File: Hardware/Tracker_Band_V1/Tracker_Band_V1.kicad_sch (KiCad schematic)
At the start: 30 parts, among them J1 USB_C_USB20, SW1 EVP-AVAA1A, SW2 EVP-AVAA1A, U1 ESP32-C3-MINI-1-N4, U2 BNO085, U3 RT8010, U4 MCP73832-2-AC, U5 LM66200, U6 IN-PI15TAT5R5G5B, X1 32.768kHz

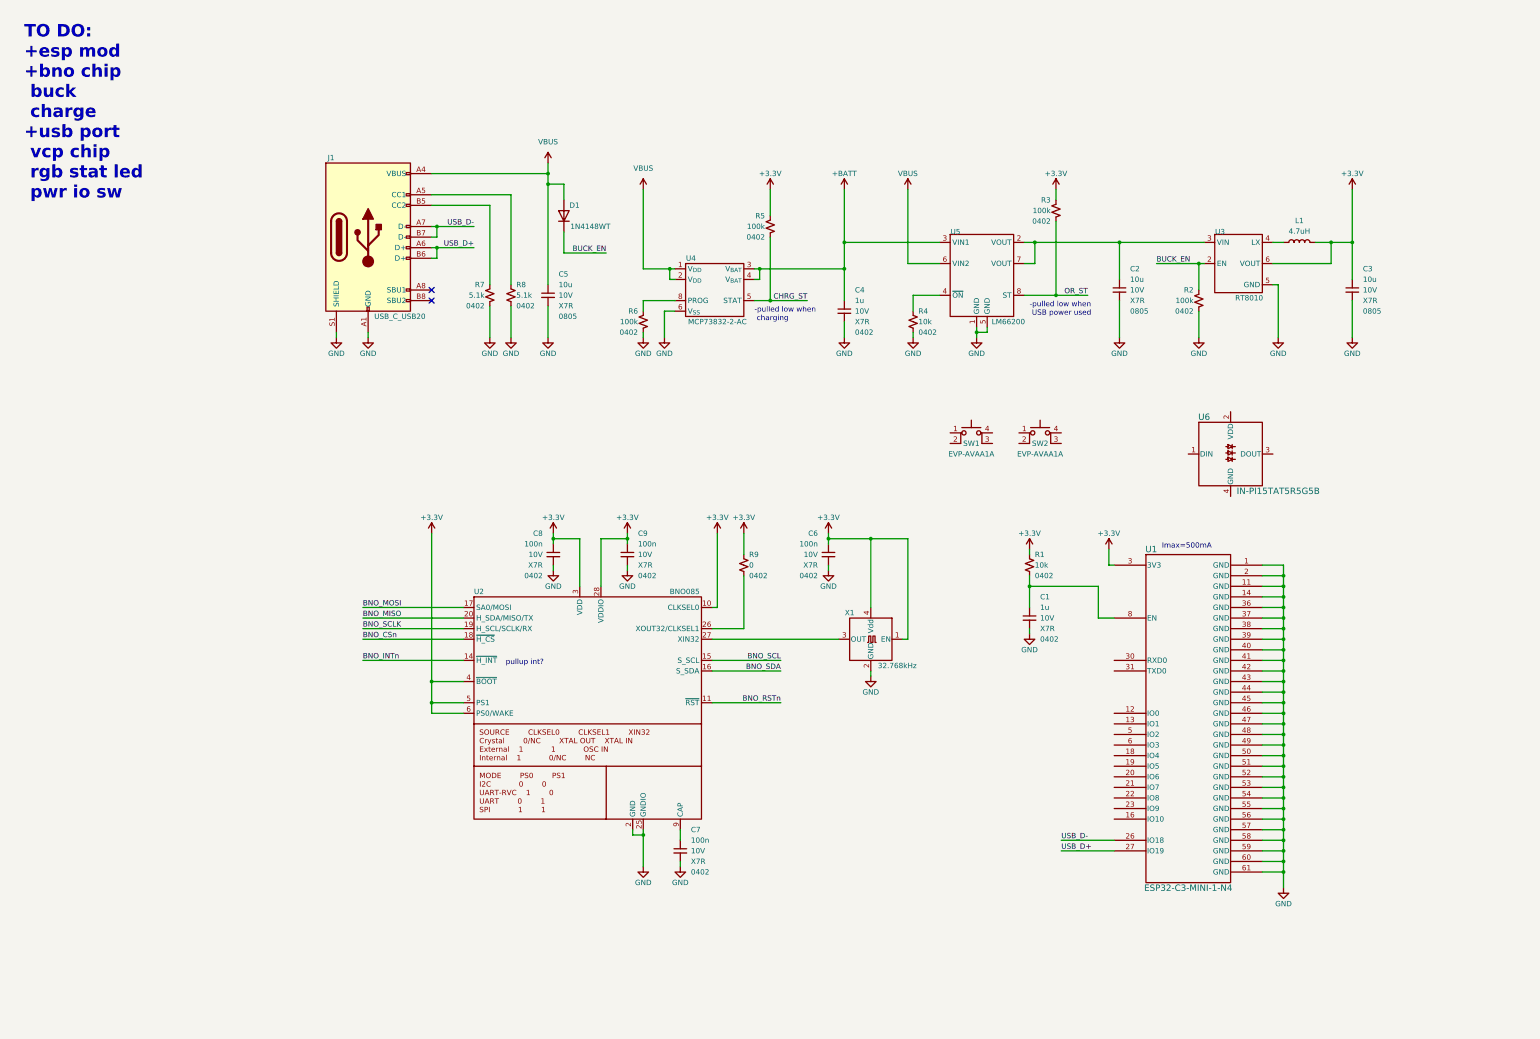
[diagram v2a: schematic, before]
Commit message: Schematic ready for layout
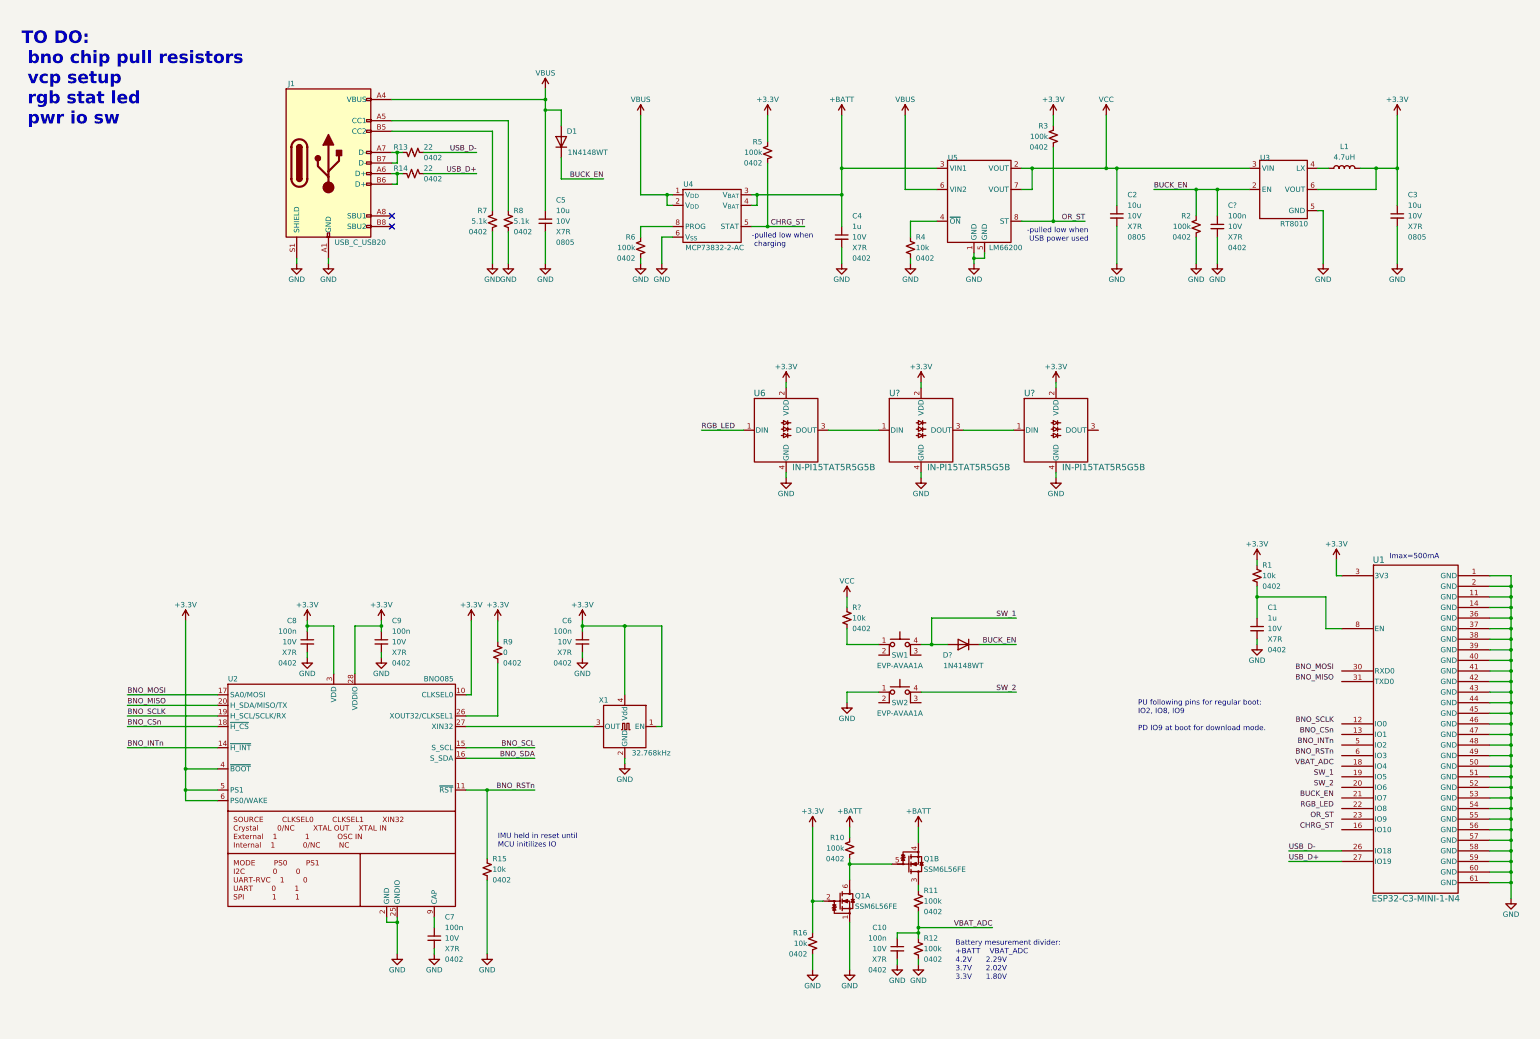
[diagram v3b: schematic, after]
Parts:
- added C10, C?: 100n, Capacitor_SMD:C_0402_1005Metric, symbol Device:C_Small
- added D?: 1N4148WT, Diode_SMD:D_SOD-523, symbol Diode:1N4148WT
- added Q1: SSM6L56FE, Package_TO_SOT_SMD:SOT-563, symbol 00_tracker_sym:SSM6L56FE
- added R10, R11, R12: 100k, Resistor_SMD:R_0402_1005Metric, symbol Device:R_Small_US
- added R13, R14: 22, Resistor_SMD:R_0402_1005Metric, symbol Device:R_Small_US
- added R15, R16, R?: 10k, Resistor_SMD:R_0402_1005Metric, symbol Device:R_Small_US
- added U? (x2): IN-PI15TAT5R5G5B, 00_tracker_fp:IN-PI15_INL, symbol 00_tracker_sym:IN-PI15TAT5R5G5B
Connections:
- net +3.3V: now also U6.2 (VDD), Q1.2 (G), R16.1, U?.2 (VDD), U?.2 (VDD)
- net +BATT: now also Q1.4 (1), R10.1
- net BNO_RSTn: now also R15.1
- net BUCK_EN: now also C?.1, D?.1 (K)
- net GND: now also SW2.1, U6.4 (GND), C10.2, C?.2, Q1.1 (S), R12.2, R15.2, R16.2, U?.4 (GND), U?.4 (GND)
- net USB_D+: now also R14.2; no longer J1.A6 (D+), J1.B6 (D+)
- net USB_D-: now also R13.2; no longer J1.A7 (D-), J1.B7 (D-)
- net SW_2: now reaches SW2.4 (A)
- net VCC: now reaches C2.1, U3.3 (VIN), U5.2 (VOUT), U5.7 (VOUT)
- net VCC: now also R?.1
- net at SW1.1: now also R?.2
- net SW_1: now reaches SW1.4 (A)
- net SW_1: now also D?.2 (A)
- net RGB_LED: now reaches U6.1 (DIN)
- net at U6.3 (DOUT): now also U?.1 (DIN)
- new net: Q1.3 (D), R11.1
- new net: Q1.5 (G), Q1.6 (D), R10.2
- new net: J1.A6 (D+), J1.B6 (D+), R14.1
- new net: J1.A7 (D-), J1.B7 (D-), R13.1
- new net: U?.1 (DIN), U?.3 (DOUT)
- new net VBAT_ADC: C10.1, R11.2, R12.1
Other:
- note added: "Battery mesurement divider: +BATT VBAT_ADC 4.2V 2.29V 3.7V 2.02V 3.3V 1.80V"
- note added: "IMU held in reset until MCU initilizes IO"
- note added: "PU following pins for regular boot: IO2, IO8, IO9 PD IO9 at boot for download mode."
- note added: "TO DO: bno chip pull resistors vcp setup rgb stat led pwr io sw"
- note removed: "TO DO: +esp mod +bno chip buck charge +usb port vcp chip rgb stat led pwr io sw"
- note removed: "pullup int?"
- moved on the sheet: C1, C2, C3, C4, C5, C6, C7, C8, C9, D1, J1, L1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

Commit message: Added ESP MCU IO details
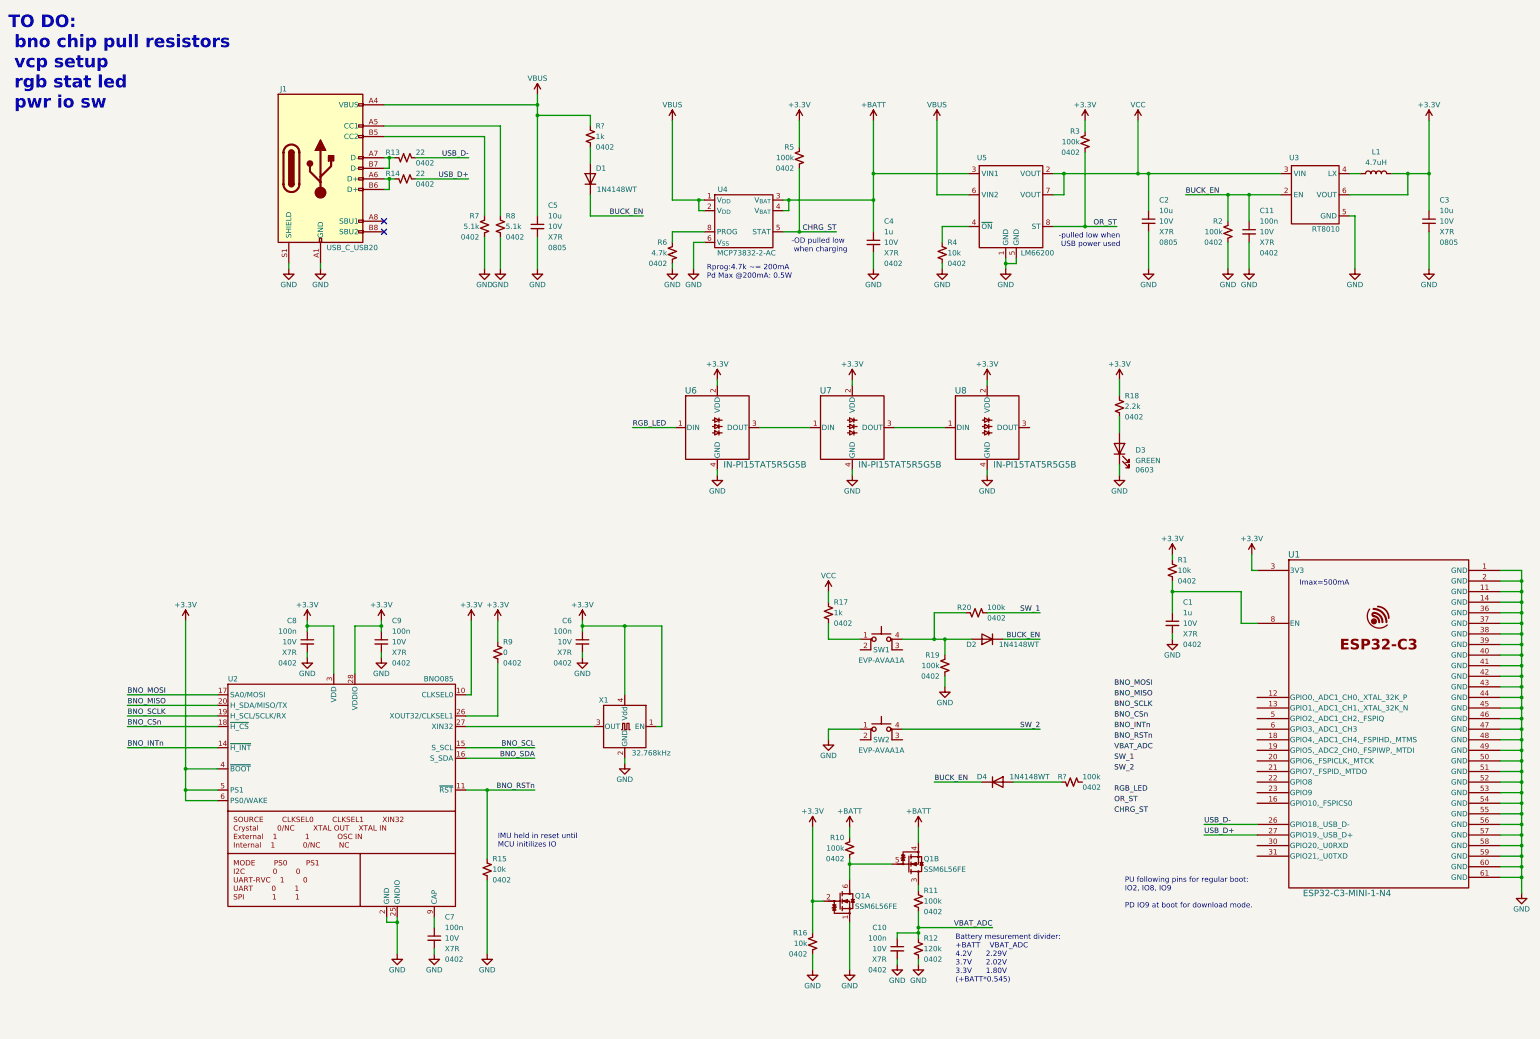
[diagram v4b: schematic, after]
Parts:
- added D3: GREEN, LED_SMD:LED_0603_1608Metric, symbol Device:LED
- added D4: 1N4148WT, Diode_SMD:D_SOD-523, symbol Diode:1N4148WT
- added R18: 2.2k, Resistor_SMD:R_0402_1005Metric, symbol Device:R_Small_US
- added R19, R20, R?: 100k, Resistor_SMD:R_0402_1005Metric, symbol Device:R_Small_US
- added R?: 1k, Resistor_SMD:R_0402_1005Metric, symbol Device:R_Small_US
- R12: value 100k -> 120k
- R17: renamed from R?; value 10k -> 1k
- R6: value 100k -> 4.7k
- gave numbers to parts that had none: 4
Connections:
- net +3.3V: now also R18.1
- net BUCK_EN: now also D4.1 (K)
- net GND: now also D3.1 (K), R19.2
- net SW_1: now also R20.2; no longer D2.2 (A), SW1.4 (A)
- net VBUS: now also R?.1; no longer D1.2 (A)
- new net: D1.2 (A), R?.2
- new net: D2.2 (A), R19.1, R20.1, SW1.4 (A)
- new net: D3.2 (A), R18.2
- new net: D4.2 (A), R?.1
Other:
- note added: "-OD pulled low when charging"
- note added: "Battery mesurement divider: +BATT VBAT_ADC 4.2V 2.29V 3.7V 2.02V 3.3V 1.80V (+BATT*0.545)"
- note added: "Rprog:4.7k ~= 200mA Pd Max @200mA: 0.5W"
- note removed: "-pulled low when charging"
- note removed: "Battery mesurement divider: +BATT VBAT_ADC 4.2V 2.29V 3.7V 2.02V 3.3V 1.80V"
- moved on the sheet: C1, C11, C2, C3, C4, C5, D1, D2, J1, L1, R1, R13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

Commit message: started layout
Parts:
- added U9: IN-PI15TAT5R5G5B, 00_tracker_fp:IN-PI15_INL, symbol 00_tracker_sym:IN-PI15TAT5R5G5B
- C4: value 1u -> 10u; footprint Capacitor_SMD:C_0402_1005Metric -> Capacitor_SMD:C_0805_2012Metric; Size 0402 -> 0805
- C5: footprint Capacitor_SMD:C_0402_1005Metric -> Capacitor_SMD:C_0805_2012Metric
- gave numbers to parts that had none: 2
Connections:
- net +3.3V: now also U9.2 (VDD)
- net GND: now also U9.4 (GND)
- net at U8.3 (DOUT): now also U9.1 (DIN)
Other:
- moved on the sheet: D3, R18, U6, U7, U8

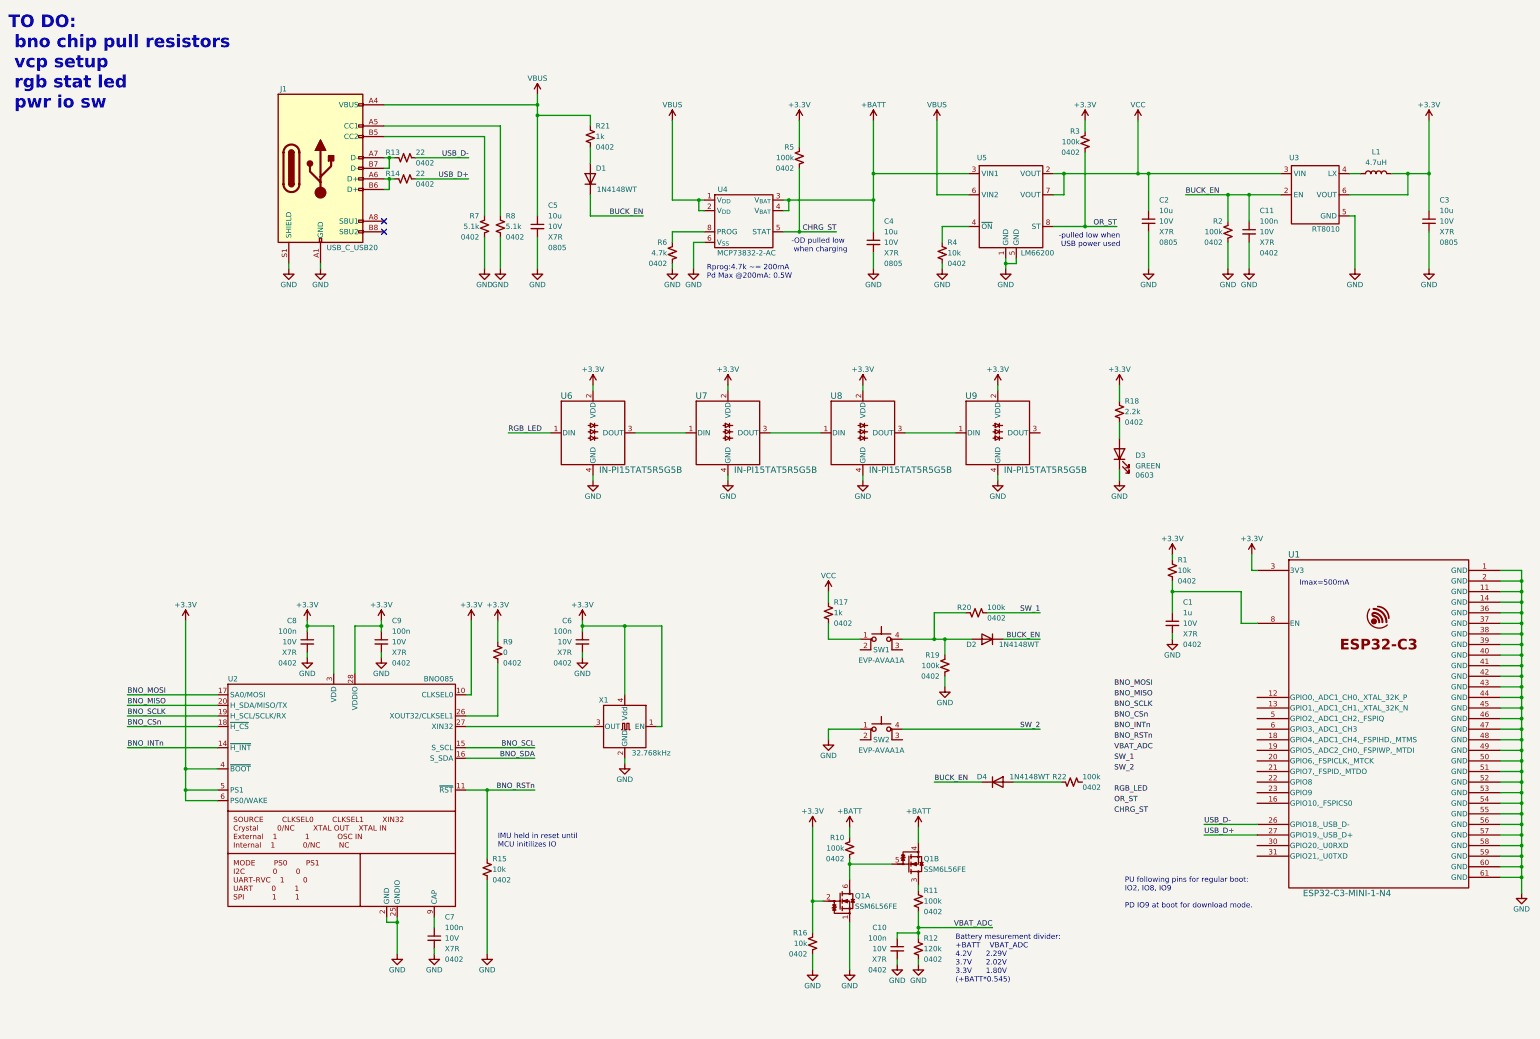
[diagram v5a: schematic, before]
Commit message: Update sch & add switch 3d model
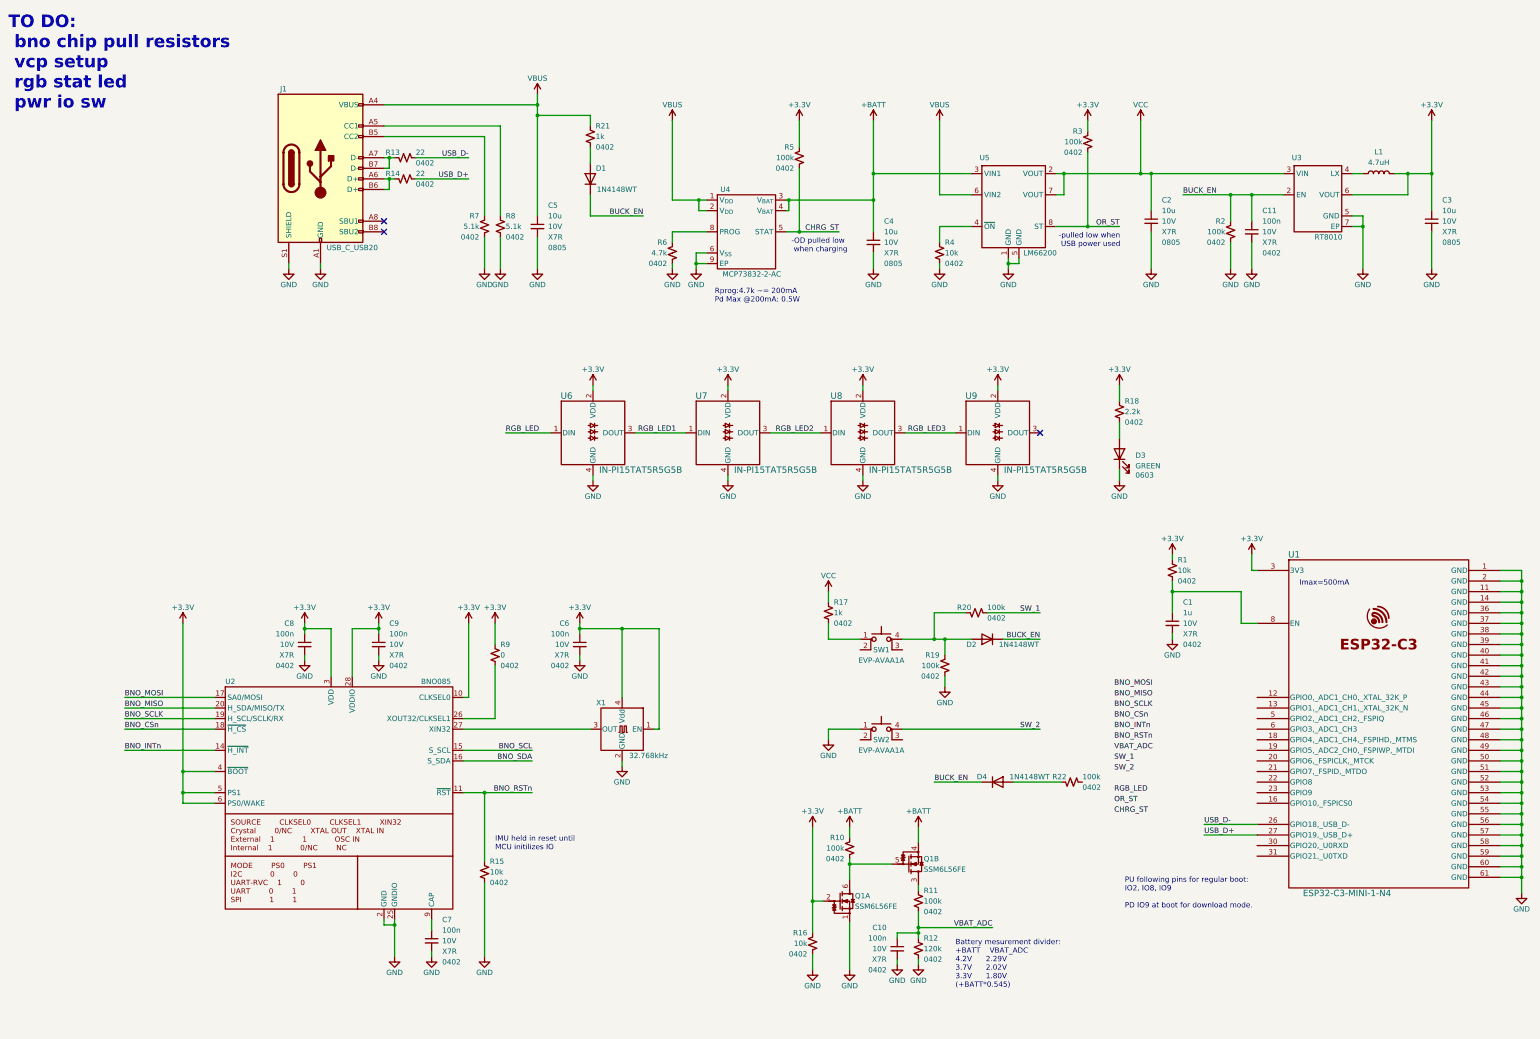
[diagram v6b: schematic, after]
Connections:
- net GND: now also U3.7 (EP), U4.9 (EP)
- net RGB_LED1: now reaches U6.3 (DOUT), U7.1 (DIN)
- net RGB_LED3: now reaches U8.3 (DOUT), U9.1 (DIN)
- net RGB_LED2: now reaches U7.3 (DOUT), U8.1 (DIN)
- no-connect marks 2 -> 3
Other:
- moved on the sheet: C11, C2, C3, C6, C7, C8, C9, L1, R15, R2, R3, R4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

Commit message: Component positioning & PCB sizing
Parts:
- removed R4: 10k, Resistor_SMD:R_0402_1005Metric, symbol Device:R_Small_US
- R22: value 100k -> 1k
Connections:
- net GND: now also U5.4 (~{ON})
- net VBAT_ADC: now also U1.6 (GPIO3,_ADC1_CH3)
- net at D2.2 (A), R19.1, R20.1: now also SW1.1, SW1.2; no longer SW1.4 (A)
- net at R17.2: now also SW1.4 (A); no longer SW1.1
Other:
- note added: "TO DO: bno chip PU resistors internal I2C ESP boot pull ressitors"
- note removed: "TO DO: bno chip pull resistors vcp setup rgb stat led pwr io sw"
- moved on the sheet: C11, C2, C3, L1, R2, R22, R3, U3, U5
